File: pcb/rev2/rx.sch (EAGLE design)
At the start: 34 parts, among them Y1 CRYSTAL-26MHZSMD-3.2X2.5

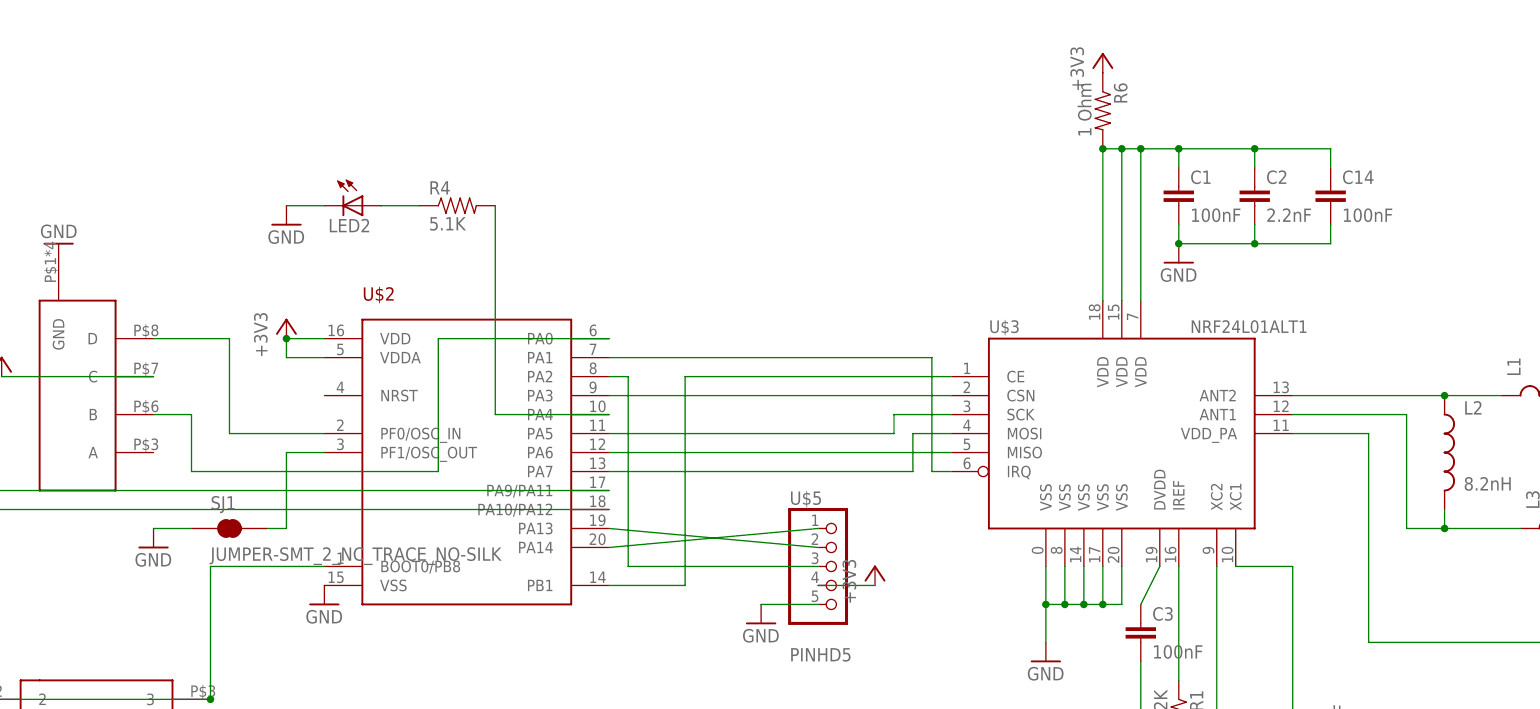
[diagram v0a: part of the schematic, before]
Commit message: added more power filtering, added RX interrupt
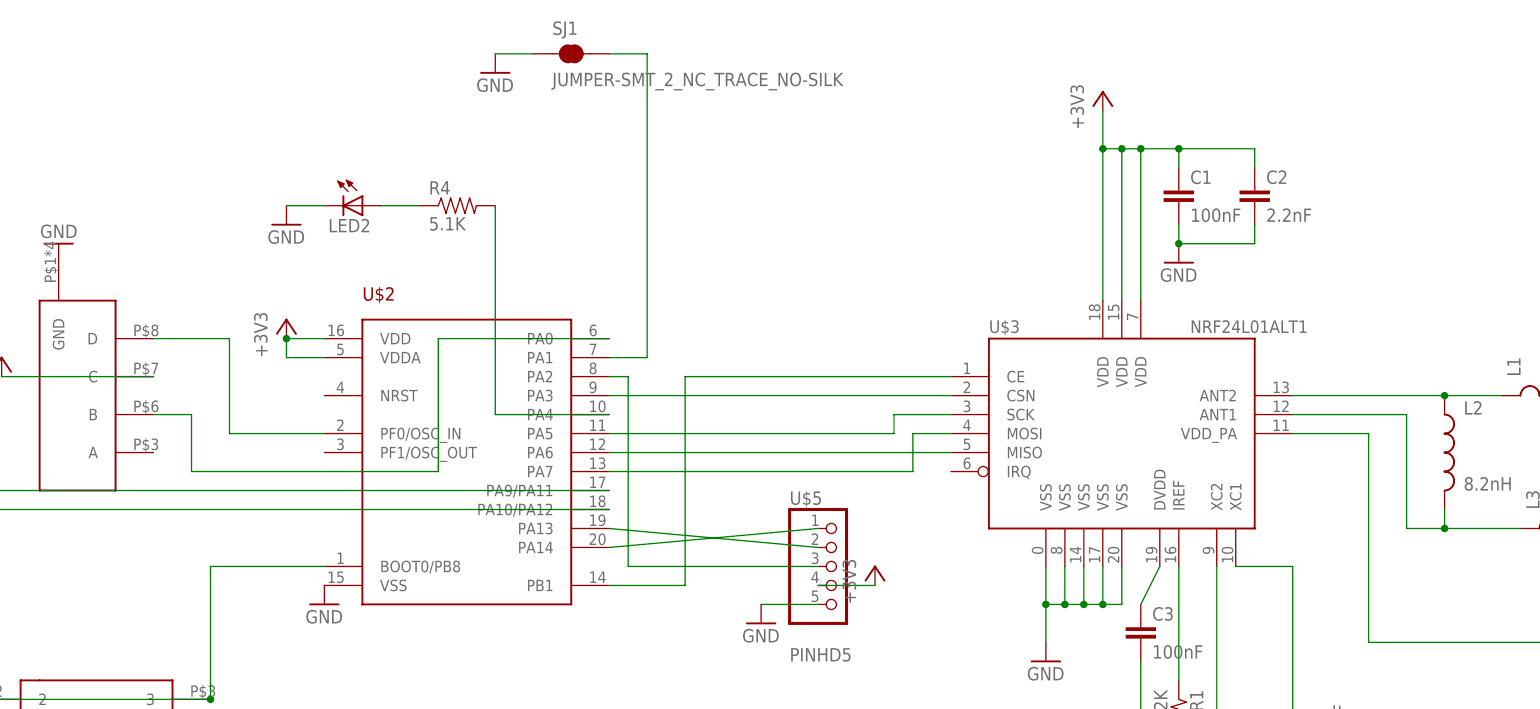
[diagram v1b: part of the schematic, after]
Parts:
- removed C14: 100nF, clock:CAP0805
- removed R6: 1 Ohm, joyAnalog:RESISTOR0805-RES
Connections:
- removed net N$28: C1.1, C14.1, C2.1, R6.2, U$3.VDD@15, U$3.VDD@18, U$3.VDD@7
- removed net N$30: U$2.PA1, U$3.IRQ
- net +3V3: now also C1.1, C2.1, U$3.VDD@15, U$3.VDD@18, U$3.VDD@7; no longer R6.1
- net GND: no longer C14.2
- net N$19: now also U$2.PA1; no longer U$2.PF1/OSC_OUT
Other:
- moved on the sheet: SJ1
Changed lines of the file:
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@@
 <part name="GND6" library="clock" deviceset="GND" device=""/>
 <part name="GND13" library="supply1" library_urn="urn:adsk.eagle:library:371" deviceset="GND" device=""/>
-<part name="R6" library="joyAnalog" deviceset="RESISTOR" device="0805-RES" value="1 Ohm"/>
-<part name="C14" library="clock" deviceset="CAP" device="0805" value="100nF"/>
 </parts>
 <sheets>
@@
 <instance part="U$1" gate="G$1" x="-22.86" y="17.78" rot="R270"/>
 <instance part="GND7" gate="1" x="-116.84" y="-25.4"/>
-<instance part="+3V1" gate="G$1" x="116.84" y="63.5"/>
+<instance part="+3V1" gate="G$1" x="116.84" y="58.42"/>
 <instance part="GND1" gate="1" x="109.22" y="-17.78"/>
 <instance part="C1" gate="G$1" x="127" y="43.18"/>
@@
 <instance part="R4" gate="G$1" x="30.48" y="43.18"/>
 <instance part="P+1" gate="1" x="-137.16" y="0"/>
-<instance part="SJ1" gate="G$1" x="0" y="0"/>
+<instance part="SJ1" gate="G$1" x="45.72" y="63.5"/>
 <instance part="U$10" gate="G$1" x="-17.78" y="-27.94"/>
 <instance part="LED2" gate="G$1" x="17.78" y="43.18" rot="R270"/>
@@
 <instance part="E1" gate="G$1" x="241.3" y="17.78" rot="R270"/>
 <instance part="GND6" gate="1" x="231.14" y="7.62"/>
-<instance part="GND13" gate="1" x="-10.16" y="-2.54"/>
-<instance part="R6" gate="G$1" x="116.84" y="55.88" rot="R270"/>
-<instance part="C14" gate="G$1" x="147.32" y="43.18"/>
+<instance part="GND13" gate="1" x="35.56" y="60.96"/>
 </instances>
 <busses>
@@
 <wire x1="137.16" y1="38.1" x2="127" y2="38.1" width="0.1524" layer="91"/>
 <junction x="127" y="38.1"/>
-<pinref part="C14" gate="G$1" pin="2"/>
-<wire x1="147.32" y1="40.64" x2="147.32" y2="38.1" width="0.1524" layer="91"/>
-<wire x1="147.32" y1="38.1" x2="137.16" y2="38.1" width="0.1524" layer="91"/>
-<junction x="137.16" y="38.1"/>
 </segment>
 <segment>
@@
 <segment>
 <pinref part="SJ1" gate="G$1" pin="1"/>
-<wire x1="-10.16" y1="0" x2="-5.08" y2="0" width="0.1524" layer="91"/>
+<wire x1="35.56" y1="63.5" x2="40.64" y2="63.5" width="0.1524" layer="91"/>
 <pinref part="GND13" gate="1" pin="GND"/>
 </segment>
 </net>
 <net name="+3V3" class="0">
+<segment>
+<pinref part="+3V1" gate="G$1" pin="+3V3"/>
+<pinref part="U$3" gate="G$1" pin="VDD@18"/>
+<wire x1="116.84" y1="55.88" x2="116.84" y2="50.8" width="0.1524" layer="91"/>
+<pinref part="U$3" gate="G$1" pin="VDD@15"/>
+<wire x1="116.84" y1="50.8" x2="116.84" y2="30.48" width="0.1524" layer="91"/>
+<wire x1="116.84" y1="50.8" x2="119.38" y2="50.8" width="0.1524" layer="91"/>
+<wire x1="119.38" y1="50.8" x2="119.38" y2="30.48" width="0.1524" layer="91"/>
+<junction x="116.84" y="50.8"/>
+<pinref part="U$3" gate="G$1" pin="VDD@7"/>
+<wire x1="119.38" y1="50.8" x2="121.92" y2="50.8" width="0.1524" layer="91"/>
+<wire x1="121.92" y1="50.8" x2="121.92" y2="30.48" width="0.1524" layer="91"/>
+<junction x="119.38" y="50.8"/>
+<pinref part="C1" gate="G$1" pin="1"/>
+<wire x1="121.92" y1="50.8" x2="127" y2="50.8" width="0.1524" layer="91"/>
+<wire x1="127" y1="50.8" x2="127" y2="48.26" width="0.1524" layer="91"/>
+<junction x="121.92" y="50.8"/>
+<pinref part="C2" gate="G$1" pin="1"/>
+<wire x1="127" y1="50.8" x2="137.16" y2="50.8" width="0.1524" layer="91"/>
+<wire x1="137.16" y1="50.8" x2="137.16" y2="48.26" width="0.1524" layer="91"/>
+<junction x="127" y="50.8"/>
+</segment>
 <segment>
 <pinref part="U$4" gate="G$1" pin="OUT"/>
@@
 <wire x1="-30.48" y1="20.32" x2="-10.16" y2="20.32" width="0.1524" layer="91"/>
 </segment>
-<segment>
-<pinref part="R6" gate="G$1" pin="1"/>
-<pinref part="+3V1" gate="G$1" pin="+3V3"/>
-</segment>
 </net>
 <net name="N$1" class="0">
@@
 </segment>
 </net>
+<net name="N$19" class="0">
+<segment>
+<pinref part="SJ1" gate="G$1" pin="2"/>
+<wire x1="55.88" y1="63.5" x2="50.8" y2="63.5" width="0.1524" layer="91"/>
+<pinref part="U$2" gate="G$1" pin="PA1"/>
+<wire x1="50.8" y1="22.86" x2="55.88" y2="22.86" width="0.1524" layer="91"/>
+<wire x1="55.88" y1="22.86" x2="55.88" y2="63.5" width="0.1524" layer="91"/>
+</segment>
+</net>
 <net name="N$14" class="0">
 <segment>
@@
 </segment>
 </net>
-<net name="N$28" class="0">
-<segment>
-<pinref part="U$3" gate="G$1" pin="VDD@18"/>
-<pinref part="U$3" gate="G$1" pin="VDD@15"/>
-<wire x1="116.84" y1="50.8" x2="116.84" y2="30.48" width="0.1524" layer="91"/>
-<wire x1="116.84" y1="50.8" x2="119.38" y2="50.8" width="0.1524" layer="91"/>
-<wire x1="119.38" y1="50.8" x2="119.38" y2="30.48" width="0.1524" layer="91"/>
-<pinref part="U$3" gate="G$1" pin="VDD@7"/>
-<wire x1="119.38" y1="50.8" x2="121.92" y2="50.8" width="0.1524" layer="91"/>
-<wire x1="121.92" y1="50.8" x2="121.92" y2="30.48" width="0.1524" layer="91"/>
-<junction x="119.38" y="50.8"/>
-<pinref part="C1" gate="G$1" pin="1"/>
-<wire x1="121.92" y1="50.8" x2="127" y2="50.8" width="0.1524" layer="91"/>
-<wire x1="127" y1="50.8" x2="127" y2="48.26" width="0.1524" layer="91"/>
-<junction x="121.92" y="50.8"/>
-<pinref part="C2" gate="G$1" pin="1"/>
-<wire x1="127" y1="50.8" x2="137.16" y2="50.8" width="0.1524" layer="91"/>
-<wire x1="137.16" y1="50.8" x2="137.16" y2="48.26" width="0.1524" layer="91"/>
-<junction x="127" y="50.8"/>
-<pinref part="R6" gate="G$1" pin="2"/>
-<junction x="116.84" y="50.8"/>
-<wire x1="137.16" y1="50.8" x2="147.32" y2="50.8" width="0.1524" layer="91"/>
-<junction x="137.16" y="50.8"/>
-<pinref part="C14" gate="G$1" pin="1"/>
-<wire x1="147.32" y1="50.8" x2="147.32" y2="48.26" width="0.1524" layer="91"/>
-</segment>
-</net>
-<net name="N$30" class="0">
-<segment>
-<pinref part="U$2" gate="G$1" pin="PA1"/>
-<pinref part="U$3" gate="G$1" pin="IRQ"/>
-<wire x1="96.52" y1="7.62" x2="93.98" y2="7.62" width="0.1524" layer="91"/>
-<wire x1="93.98" y1="7.62" x2="93.98" y2="22.86" width="0.1524" layer="91"/>
-<wire x1="93.98" y1="22.86" x2="50.8" y2="22.86" width="0.1524" layer="91"/>
-</segment>
-</net>
-<net name="N$19" class="0">
-<segment>
-<pinref part="U$2" gate="G$1" pin="PF1/OSC_OUT"/>
-<wire x1="12.7" y1="10.16" x2="7.62" y2="10.16" width="0.1524" layer="91"/>
-<wire x1="7.62" y1="10.16" x2="7.62" y2="0" width="0.1524" layer="91"/>
-<pinref part="SJ1" gate="G$1" pin="2"/>
-<wire x1="7.62" y1="0" x2="5.08" y2="0" width="0.1524" layer="91"/>
-</segment>
-</net>
